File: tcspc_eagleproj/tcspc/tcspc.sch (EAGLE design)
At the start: 10 parts, among them U1 THS788, U2 MCP4725, U3 MCP4725, U4 MCP4725, U5 MCP4725, X1 SMA, X2 SMA, X3 SMA, X4 SMA

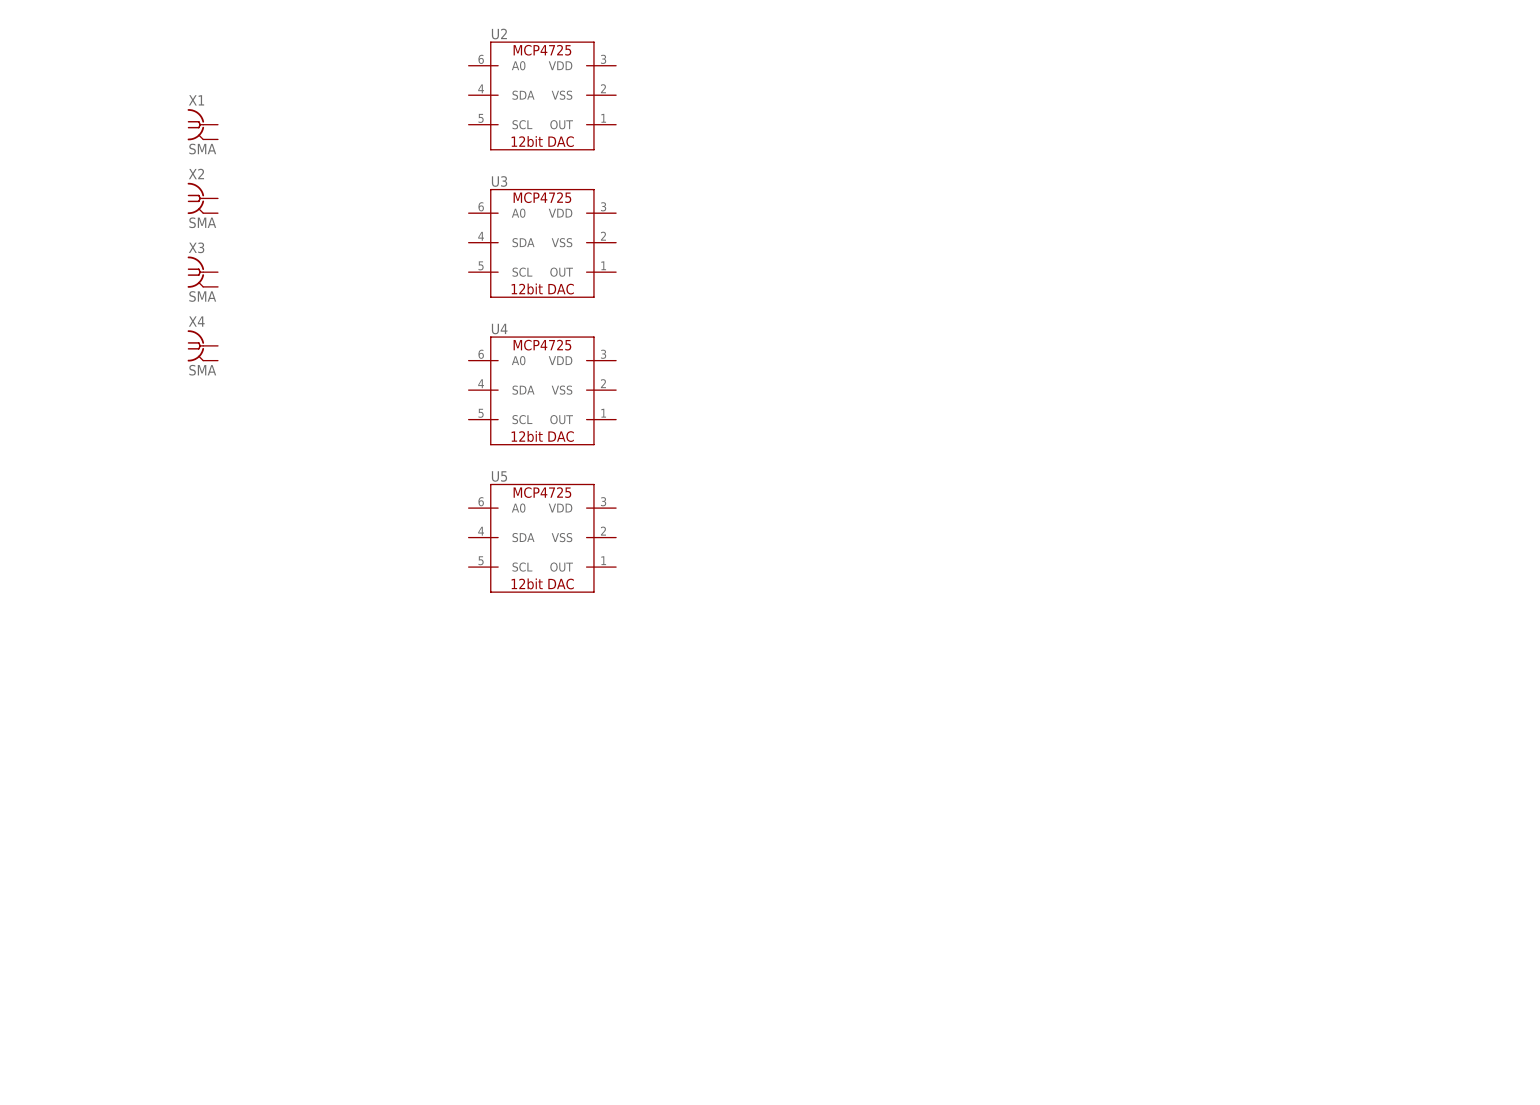
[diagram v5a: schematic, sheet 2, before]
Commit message: Added 0402 option to the library, tweaked the front end, organized and ordered the front end on the board, added a bunch of bypass caps for the TDC.
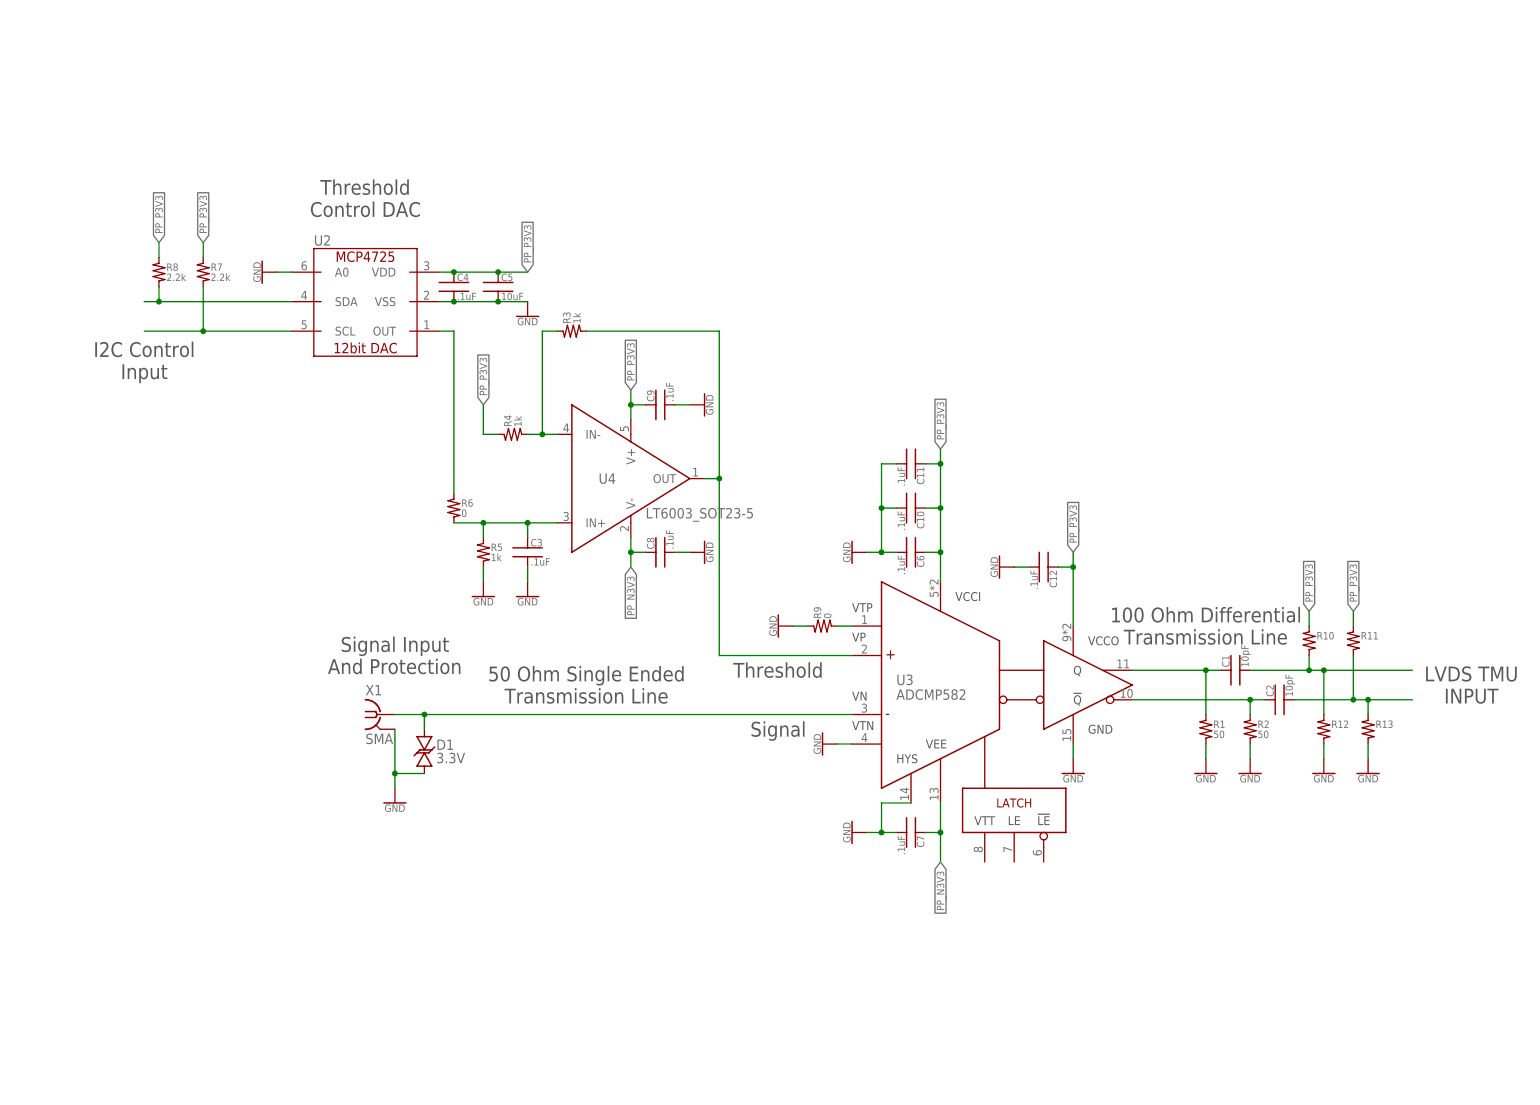
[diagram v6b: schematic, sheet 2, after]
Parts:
- removed U5: MCP4725, tcspc_lib:MCP4725
- removed X2, X3, X4: SMA, tcspc_lib:SMA
- added C1, C2: 10pF, tcspc_lib:CAP_0402
- added C10, C11, C12, C3, C4, C47, C6, C7, C8, C9: .1uF, tcspc_lib:CAP_0603
- added C13, C15, C17, C19, C21, C23, C25, C27, C29, C31, C33, C35, C37, C39, C41, C43, C45: .1uF, tcspc_lib:CAP_0402
- added C14, C16, C18, C20, C22, C24, C26, C28, C30, C32, C34, C36, C38, C40, C42, C44, C46: 10nF, tcspc_lib:CAP_0402
- added C48, C49, C50, C51: 1uF, tcspc_lib:CAP_0603
- added C5: 10uF, tcspc_lib:CAP_0603
- added D1: 3.3V, tcspc_lib:TVS-BI_DO-214AA
- added R1, R2: 50, tcspc_lib:RES_0402
- added R10, R11, R12, R13: (no value), tcspc_lib:RES_0402
- added R3, R4, R5: 1k, tcspc_lib:RES_0603
- added R6: 0, tcspc_lib:RES_0603
- added R7, R8: 2.2k, tcspc_lib:RES_0603
- added R9: 0, tcspc_lib:RES_0402
- U3: value MCP4725 -> ADCMP582; device tcspc_lib:MCP4725 -> tcspc_lib:ADCMP582
- U4: value MCP4725 -> LT6003_SOT23-5; device tcspc_lib:MCP4725 -> tcspc_lib:LT6003_SOT23-5
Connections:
- new net !TMU_DOUT_A: U1.!RDATA-A
- new net !TMU_IN_A: U1.!EVENT-A
- new net !TMU_IN_B: U1.!EVENT-B
- new net !TMU_IN_C: U1.!EVENT-C
- new net !TMU_IN_D: U1.!EVENT-D
- new net GND: C10.2, C11.2, C12.2, C13.2, C14.2, C15.2, C16.2, C17.2, C18.2, C19.2, C20.2, C21.2, C22.2, C23.2, C24.2, C25.2, C26.2, C27.2, C28.2, C29.2, C3.2, C30.2, C31.2, C32.2, C33.2, C34.2, C35.2, C36.2, C37.2, C38.2, C39.2, C4.2, C40.2, C41.2, C42.2, C43.2, C44.2, C45.2, C46.2, C47.2, C48.2, C49.2, C5.2, C50.2, C51.2, C6.2, C7.2, C8.2, C9.2, D1.A2, G1.GND, R1.2, R12.2, R13.2, R2.2, R5.2, R9.1, U1.GND, U2.A0, U2.VSS, U3.GND, U3.HYS, U3.VTN, X1.GND
- new net N$10: U1.TEMP
- new net N$11: U1.OT_ALRM
- new net N$12: R3.1, R4.2, U4.IN-
- new net N$13: R3.2, U3.VP, U4.OUT
- new net N$14: U1.!RESET
- new net N$15: U1.HDATA
- new net N$16: U1.HCLK
- new net N$17: U1.!HSTROBE
- new net N$18: D1.A1, U3.VN, X1.1
- new net N$19: R7.2, U2.SCL
- new net N$20: R8.2, U2.SDA
- new net N$21: U1.!RSTROBE-D
- new net N$22: U1.RSTROBE-D
- new net N$23: U1.!RSTROBE-C
- new net N$24: U1.RSTROBE-C
- new net N$25: U1.!RSTROBE-B
- new net N$26: U1.RSTROBE-B
- new net N$27: U1.!RSTROBE-A
- new net N$28: U1.RSTROBE-A
- new net N$29: U1.!RCLK
- new net N$3: C2.1, R2.1, U3.!Q
- new net N$30: U1.RCLK
- new net N$31: U1.!RDATA-D
- new net N$32: U1.RDATA-D
- new net N$33: U1.!RDATA-C
- new net N$34: U1.RDATA-C
- new net N$35: U1.!RDATA-B
- new net N$36: U1.RDATA-B
- new net N$4: C1.2, R10.2, R12.1
- new net N$5: C2.2, R11.2, R13.1
- new net N$6: C1.1, R1.1, U3.Q
- new net N$7: R9.2, U3.VTP
- new net N$8: R6.1, U2.OUT
- new net N$9: C3.1, R5.1, R6.2, U4.IN+
- new net PP_N3V3: C7.1, C8.1, U3.VEE, U4.V-
- new net PP_P3V3: C10.1, C11.1, C12.1, C13.1, C14.1, C15.1, C16.1, C17.1, C18.1, C19.1, C20.1, C21.1, C22.1, C23.1, C24.1, C25.1, C26.1, C27.1, C28.1, C29.1, C30.1, C31.1, C32.1, C33.1, C34.1, C35.1, C36.1, C37.1, C38.1, C39.1, C4.1, C40.1, C41.1, C42.1, C43.1, C44.1, C45.1, C46.1, C47.1, C48.1, C49.1, C5.1, C50.1, C51.1, C6.1, C9.1, G1.VDD, R10.1, R11.1, R4.1, R7.1, R8.1, U1.VCC, U2.VDD, U3.VCCI, U3.VCCO, U4.V+
- new net TMU_DOUT_A: U1.RDATA-A
- new net TMU_IN_A: U1.EVENT-A
- new net TMU_IN_B: U1.EVENT-B
- new net TMU_IN_C: U1.EVENT-C
- new net TMU_IN_D: U1.EVENT-D
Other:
- note added: "100 Ohm Differential Transmission Line"
- note added: "100_OHM_DIFF"
- note added: "50 Ohm Single Ended Transmission Line"
- note added: "50_OHM_SE"
- note added: "I2C Control Input"
- note added: "LVDS TMU INPUT"
- note added: "Signal"
- note added: "Signal Input And Protection"
- note added: "Threshold"
- note added: "Threshold Control DAC"
- moved on the sheet: U2, X1

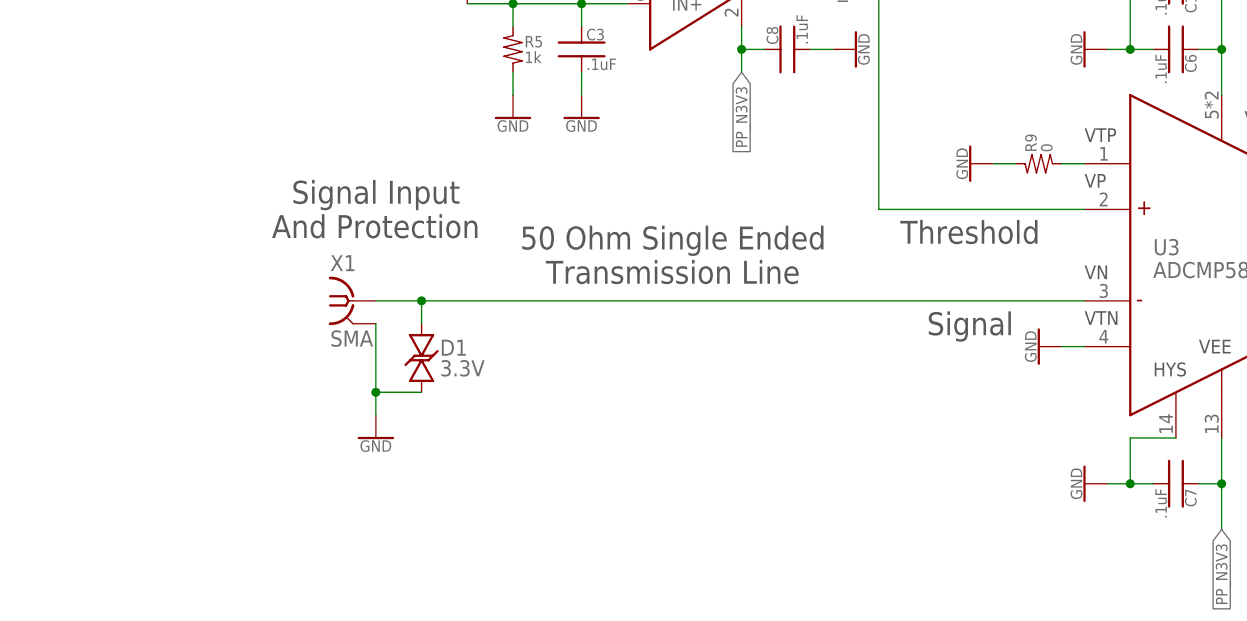
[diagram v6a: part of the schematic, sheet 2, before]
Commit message: Modified the 0402 package to have layout indicators, so I can leave myself some room for when I assemble the board. Twiddled the layout of the frontend, so that I can try get a frontend demo board out the door.
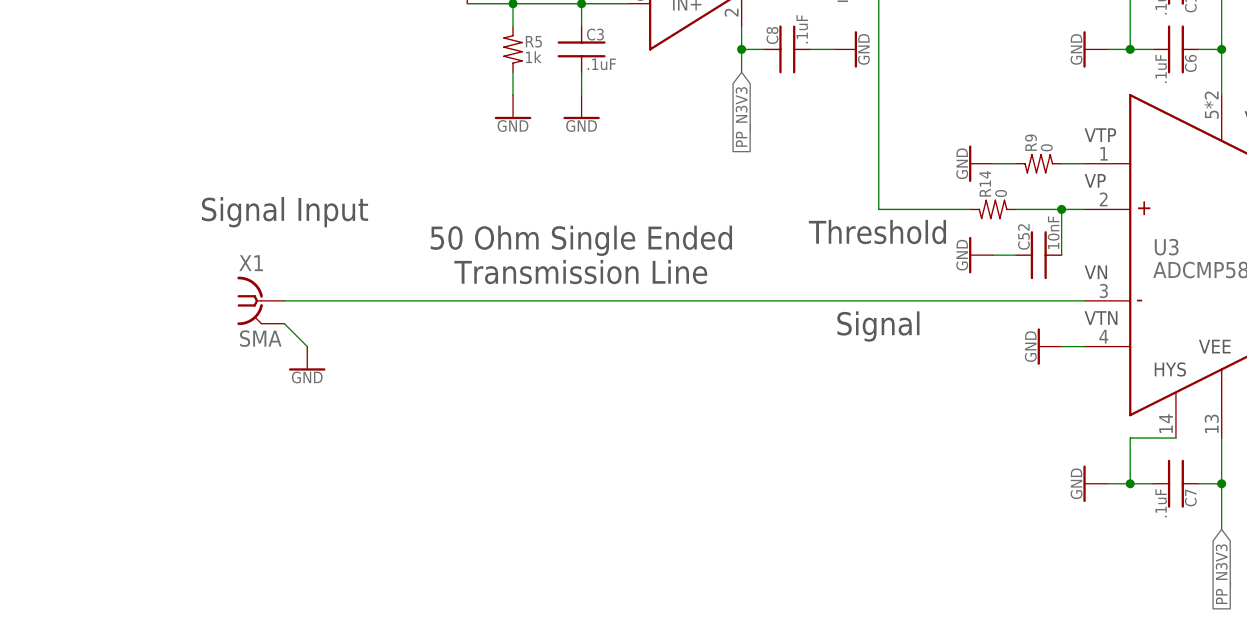
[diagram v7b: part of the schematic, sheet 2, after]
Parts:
- removed D1: 3.3V, tcspc_lib:TVS-BI_DO-214AA
- added C52: 10nF, tcspc_lib:CAP_0402
- added R14: 0, tcspc_lib:RES_0402
- C10, C11, C12, C6, C7: device tcspc_lib:CAP_0603 -> tcspc_lib:CAP_0402
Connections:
- new net N$37: C52.2, R14.2, U3.VP
- net GND: now also C52.1; no longer D1.A2
- net N$13: now also R14.1; no longer U3.VP
- net N$18: no longer D1.A1
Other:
- note added: "Signal Input"
- note removed: "Signal Input And Protection"
- moved on the sheet: X1
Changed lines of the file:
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@@
 <part name="R8" library="tcspc_lib" deviceset="RES" device="_0603" value="2.2k"/>
 <part name="GND9" library="tcspc_lib" deviceset="GND" device=""/>
-<part name="D1" library="tcspc_lib" deviceset="TVS-BI" device="_DO-214AA" value="3.3V"/>
 <part name="GND10" library="tcspc_lib" deviceset="GND" device=""/>
 <part name="R9" library="tcspc_lib" deviceset="RES" device="_0402" value="0"/>
@@
 <part name="GND11" library="tcspc_lib" deviceset="GND" device=""/>
 <part name="GND12" library="tcspc_lib" deviceset="GND" device=""/>
-<part name="C6" library="tcspc_lib" deviceset="CAP" device="_0603" value=".1uF"/>
+<part name="C6" library="tcspc_lib" deviceset="CAP" device="_0402" value=".1uF"/>
 <part name="GND13" library="tcspc_lib" deviceset="GND" device=""/>
 <part name="GND14" library="tcspc_lib" deviceset="GND" device=""/>
-<part name="C7" library="tcspc_lib" deviceset="CAP" device="_0603" value=".1uF"/>
+<part name="C7" library="tcspc_lib" deviceset="CAP" device="_0402" value=".1uF"/>
 <part name="C8" library="tcspc_lib" deviceset="CAP" device="_0603" value=".1uF"/>
 <part name="C9" library="tcspc_lib" deviceset="CAP" device="_0603" value=".1uF"/>
 <part name="GND15" library="tcspc_lib" deviceset="GND" device=""/>
 <part name="GND16" library="tcspc_lib" deviceset="GND" device=""/>
-<part name="C10" library="tcspc_lib" deviceset="CAP" device="_0603" value=".1uF"/>
-<part name="C11" library="tcspc_lib" deviceset="CAP" device="_0603" value=".1uF"/>
-<part name="C12" library="tcspc_lib" deviceset="CAP" device="_0603" value=".1uF"/>
+<part name="C10" library="tcspc_lib" deviceset="CAP" device="_0402" value=".1uF"/>
+<part name="C11" library="tcspc_lib" deviceset="CAP" device="_0402" value=".1uF"/>
+<part name="C12" library="tcspc_lib" deviceset="CAP" device="_0402" value=".1uF"/>
 <part name="GND17" library="tcspc_lib" deviceset="GND" device=""/>
 <part name="C13" library="tcspc_lib" deviceset="CAP" device="_0402" value=".1uF"/>
@@
 <part name="GND22" library="tcspc_lib" deviceset="GND" device=""/>
 <part name="GND23" library="tcspc_lib" deviceset="GND" device=""/>
+<part name="C52" library="tcspc_lib" deviceset="CAP" device="_0402" value="10nF"/>
+<part name="GND24" library="tcspc_lib" deviceset="GND" device=""/>
+<part name="R14" library="tcspc_lib" deviceset="RES" device="_0402" value="0"/>
 </parts>
 <sheets>
@@
 <text x="256.54" y="91.44" size="2.54" layer="97" align="center">LVDS TMU
 INPUT</text>
-<text x="137.16" y="93.98" size="2.54" layer="97" align="center">Threshold</text>
+<text x="127" y="93.98" size="2.54" layer="97" align="center">Threshold</text>
 <text x="66.04" y="175.26" size="2.54" layer="97" align="center">Threshold
 Control DAC</text>
 <text x="27.94" y="147.32" size="2.54" layer="97" align="center">I2C Control
 Input</text>
-<text x="71.12" y="96.52" size="2.54" layer="97" align="center">Signal Input
-And Protection</text>
+<text x="60.96" y="96.52" size="2.54" layer="97" align="center">Signal Input</text>
 <text x="210.82" y="101.6" size="2.54" layer="97" align="center">100 Ohm Differential
 Transmission Line</text>
-<text x="104.14" y="91.44" size="2.54" layer="97" align="center">50 Ohm Single Ended
+<text x="93.98" y="91.44" size="2.54" layer="97" align="center">50 Ohm Single Ended
 Transmission Line</text>
 <text x="204.47" y="94.488" size="0.635" layer="203" align="bottom-center">100_OHM_DIFF</text>
 <text x="204.47" y="89.408" size="0.635" layer="203" align="bottom-center">100_OHM_DIFF</text>
-<text x="104.14" y="86.868" size="0.635" layer="203" align="bottom-center">50_OHM_SE</text>
-<text x="137.16" y="83.82" size="2.54" layer="97" align="center">Signal</text>
+<text x="93.98" y="86.868" size="0.635" layer="203" align="bottom-center">50_OHM_SE</text>
+<text x="127" y="83.82" size="2.54" layer="97" align="center">Signal</text>
 <text x="242.57" y="94.488" size="0.635" layer="203" align="bottom-center">100_OHM_DIFF</text>
 <text x="242.57" y="89.408" size="0.635" layer="203" align="bottom-center">100_OHM_DIFF</text>
@@
 <instance part="FRAME2" gate="G$1" x="0" y="0"/>
 <instance part="FRAME2" gate="G$2" x="172.72" y="0"/>
-<instance part="X1" gate="G$1" x="68.58" y="86.36"/>
+<instance part="X1" gate="G$1" x="58.42" y="86.36"/>
 <instance part="U2" gate="G$1" x="66.04" y="157.48"/>
 <instance part="U3" gate="G$1" x="172.72" y="91.44"/>
@@
 <instance part="R8" gate="G$1" x="30.48" y="162.56"/>
 <instance part="GND9" gate="1" x="48.26" y="162.56" rot="R270"/>
-<instance part="D1" gate="G$1" x="76.2" y="81.28"/>
-<instance part="GND10" gate="1" x="71.12" y="71.12"/>
+<instance part="GND10" gate="1" x="63.5" y="78.74"/>
 <instance part="R9" gate="G$1" x="144.78" y="101.6" rot="R90"/>
 <instance part="R10" gate="G$1" x="228.6" y="99.06"/>
@@
 <instance part="C12" gate="G$1" x="182.88" y="111.76" rot="R270"/>
 <instance part="GND17" gate="1" x="175.26" y="111.76" rot="R270"/>
+<instance part="C52" gate="G$1" x="144.78" y="91.44" rot="R90"/>
+<instance part="GND24" gate="1" x="137.16" y="91.44" rot="R270"/>
+<instance part="R14" gate="G$1" x="139.7" y="96.52" rot="R90"/>
 </instances>
 <busses>
@@
 <pinref part="X1" gate="G$1" pin="GND"/>
 <pinref part="GND10" gate="1" pin="GND"/>
-<wire x1="71.12" y1="83.82" x2="71.12" y2="76.2" width="0.1524" layer="91"/>
-<pinref part="D1" gate="G$1" pin="A2"/>
-<wire x1="71.12" y1="76.2" x2="71.12" y2="73.66" width="0.1524" layer="91"/>
-<wire x1="76.2" y1="76.2" x2="71.12" y2="76.2" width="0.1524" layer="91"/>
-<junction x="71.12" y="76.2"/>
+<wire x1="60.96" y1="83.82" x2="63.5" y2="81.28" width="0.1524" layer="91"/>
 </segment>
 <segment>
@@
 <wire x1="177.8" y1="111.76" x2="180.34" y2="111.76" width="0.1524" layer="91"/>
 </segment>
+<segment>
+<pinref part="GND24" gate="1" pin="GND"/>
+<pinref part="C52" gate="G$1" pin="1"/>
+<wire x1="139.7" y1="91.44" x2="142.24" y2="91.44" width="0.1524" layer="91"/>
+</segment>
 </net>
 <net name="N$3" class="2">
@@
 <wire x1="127" y1="127" x2="127" y2="96.52" width="0.1524" layer="91"/>
 <junction x="127" y="127"/>
-<pinref part="U3" gate="G$1" pin="VP"/>
-<wire x1="127" y1="96.52" x2="149.86" y2="96.52" width="0.1524" layer="91"/>
+<pinref part="R14" gate="G$1" pin="1"/>
+<wire x1="127" y1="96.52" x2="137.16" y2="96.52" width="0.1524" layer="91"/>
 </segment>
 </net>
@@
 <segment>
 <pinref part="X1" gate="G$1" pin="1"/>
-<wire x1="71.12" y1="86.36" x2="76.2" y2="86.36" width="0.1524" layer="91"/>
-<pinref part="D1" gate="G$1" pin="A1"/>
-<wire x1="76.2" y1="86.36" x2="76.2" y2="83.82" width="0.1524" layer="91"/>
-<wire x1="76.2" y1="86.36" x2="149.86" y2="86.36" width="0.1524" layer="91"/>
-<junction x="76.2" y="86.36"/>
+<wire x1="60.96" y1="86.36" x2="149.86" y2="86.36" width="0.1524" layer="91"/>
 <pinref part="U3" gate="G$1" pin="VN"/>
 </segment>
@@
 </segment>
 </net>
+<net name="N$37" class="0">
+<segment>
+<pinref part="U3" gate="G$1" pin="VP"/>
+<wire x1="147.32" y1="96.52" x2="149.86" y2="96.52" width="0.1524" layer="91"/>
+<pinref part="C52" gate="G$1" pin="2"/>
+<wire x1="147.32" y1="91.44" x2="147.32" y2="96.52" width="0.1524" layer="91"/>
+<pinref part="R14" gate="G$1" pin="2"/>
+<wire x1="142.24" y1="96.52" x2="147.32" y2="96.52" width="0.1524" layer="91"/>
+<junction x="147.32" y="96.52"/>
+</segment>
+</net>
